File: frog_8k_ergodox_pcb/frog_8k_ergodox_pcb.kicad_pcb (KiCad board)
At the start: 2 copper layers, 344.7 x 123.6 mm, 214 parts, among them J1 USB_C_Receptacle_USB2.0_14P, J10 Conn_01x01_Pin, J2 Conn_01x04_Pin, J3 Conn_01x01_Pin, J4 Conn_01x01_Pin, J5 Conn_01x01_Pin, J6 Conn_01x01_Pin, J7 Conn_01x01_Pin, J8 Conn_01x01_Pin, J9 Conn_01x01_Pin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

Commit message: Connect PMW3360 pins.
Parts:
- moved R7 45.0 mm to (363.0, 117.2), turned to 0 degrees
- moved C1 29.1 mm to (343.8, 152.5)
- moved C2 27.0 mm to (343.8, 150.2)
- moved C3 7.79 mm to (337.8, 154.2)
- moved U3 6.57 mm to (343.0, 156.8)
- moved C4 6.45 mm to (344.2, 161.8)
- moved R3 5.15 mm to (364.5, 151.2), turned to 0 degrees
- moved R1 2.61 mm to (344.8, 143.2)
- moved R2 1.25 mm to (365.5, 137.2), turned to -45 degrees
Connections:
- C3 pad 1: V_{IN 3.3V} -> +3V3
- R1 pad 1: V_{IO VDD~3.3V} -> +3V3
- R2 pad 1: V_{IO VDD~3.3V} -> +3V3
- U1 pad 5: V_{IO VDD~3.3V} -> +3V3
- U3 pad 1: V_{IN 3.3V} -> +3V3
- U3 pad 3: V_{IN 3.3V} -> +3V3
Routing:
- net +3V3: track 64.8 -> 153.5 mm, vias 0 -> 2
- net VDD_{1.8V~2.1V}: track 0.00 -> 51.8 mm
- net Net-(U1-VDDPIX): track 0.00 -> 8.92 mm
- net Net-(U1-LED_P): track 0.00 -> 3.52 mm
- net Net-(U1-~{RESET}): track 6.34 -> 3.59 mm
- net MISO_{GPIO-PMW3360}: track 47.1 -> 44.7 mm
- net BOOT-1: track 12.9 -> 14.9 mm
- net CS_{GPIO-PMW3360}: track 40.0 -> 38.6 mm, vias 2 -> 1
- net SCLK_{GPIO-PMW3360}: track 34.2 -> 33.2 mm

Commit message: Connected All nets.
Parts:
- moved J3 53.1 mm to (330.0, 159.5)
- moved J5 52.6 mm to (327.0, 159.5)
- moved J7 52.1 mm to (324.0, 159.5)
- moved J9 51.7 mm to (321.0, 159.5)
- moved J4 32.5 mm to (330.0, 163.5)
- moved J10 32.5 mm to (321.0, 163.5)
- moved J6 32.5 mm to (327.0, 163.5)
- moved J8 32.5 mm to (324.0, 163.5)
- moved C4 1.90 mm to (342.5, 161.0), turned to -135 degrees
- moved C11 1.06 mm to (352.0, 128.2)
- moved C7 0.69 mm to (341.2, 124.5)
- moved C8 0.35 mm to (345.8, 115.5)
- moved C9 0.31 mm to (354.5, 119.8)
- turned C6 to 0 degrees
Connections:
- U2 pad 10: COL16 -> ADD2
- U2 pad 11: COL15 -> ADD4
- U2 pad 12: ROW5 -> ADD6
- U2 pad 18: COL0 -> COL11
- U2 pad 19: COL1 -> COL10
- U2 pad 2: ROW2 -> ADD7
- U2 pad 20: COL2 -> COL9
- U2 pad 21: COL10 -> COL8
- U2 pad 22: COL11 -> COL7
- U2 pad 25: ADD7 -> COL6
- U2 pad 26: ADD6 -> COL5
- U2 pad 27: ADD5 -> COL4
- U2 pad 28: ADD4 -> COL3
- U2 pad 29: ADD3 -> COL2
- U2 pad 3: ROW3 -> ADD5
- U2 pad 30: ADD2 -> COL1
- U2 pad 31: ADD1 -> COL0
- U2 pad 34: ADD0 -> ROW0
- U2 pad 37: COL14 -> COL13
- U2 pad 38: COL13 -> COL14
- U2 pad 39: COL3 -> COL15
- U2 pad 4: ROW4 -> ADD3
- U2 pad 40: COL4 -> COL16
- U2 pad 41: COL5 -> ROW5
- U2 pad 42: COL6 -> ROW4
- U2 pad 43: COL7 -> ROW3
- U2 pad 45: COL8 -> ROW2
- U2 pad 46: COL9 -> ROW1
- U2 pad 5: ROW0 -> ADD1
- U2 pad 6: ROW1 -> ADD0
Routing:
- net COL0: track 103.5 -> 427.4 mm, vias 0 -> 3
- net COL1: track 58.7 -> 366.3 mm, vias 0 -> 3
- net COL2: track 105.9 -> 388.9 mm, vias 0 -> 3
- net COL3: track 105.7 -> 368.9 mm, vias 0 -> 3
- net COL4: track 104.9 -> 347.1 mm, vias 0 -> 3
- net COL5: track 105.4 -> 326.1 mm, vias 0 -> 3
- net COL6: track 106.5 -> 303.7 mm, vias 0 -> 3
- net COL7: track 102.1 -> 276.1 mm, vias 0 -> 1
- net ROW5: track 315.4 -> 484.4 mm, vias 0 -> 2
- net ROW1: track 257.2 -> 425.0 mm, vias 0 -> 2
- net ROW4: track 317.1 -> 480.1 mm
- net COL8: track 103.3 -> 258.7 mm, vias 0 -> 1
- net ROW2: track 265.8 -> 417.2 mm, vias 0 -> 2
- net ROW3: track 259.7 -> 403.2 mm
- net COL9: track 103.1 -> 240.2 mm, vias 0 -> 1
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
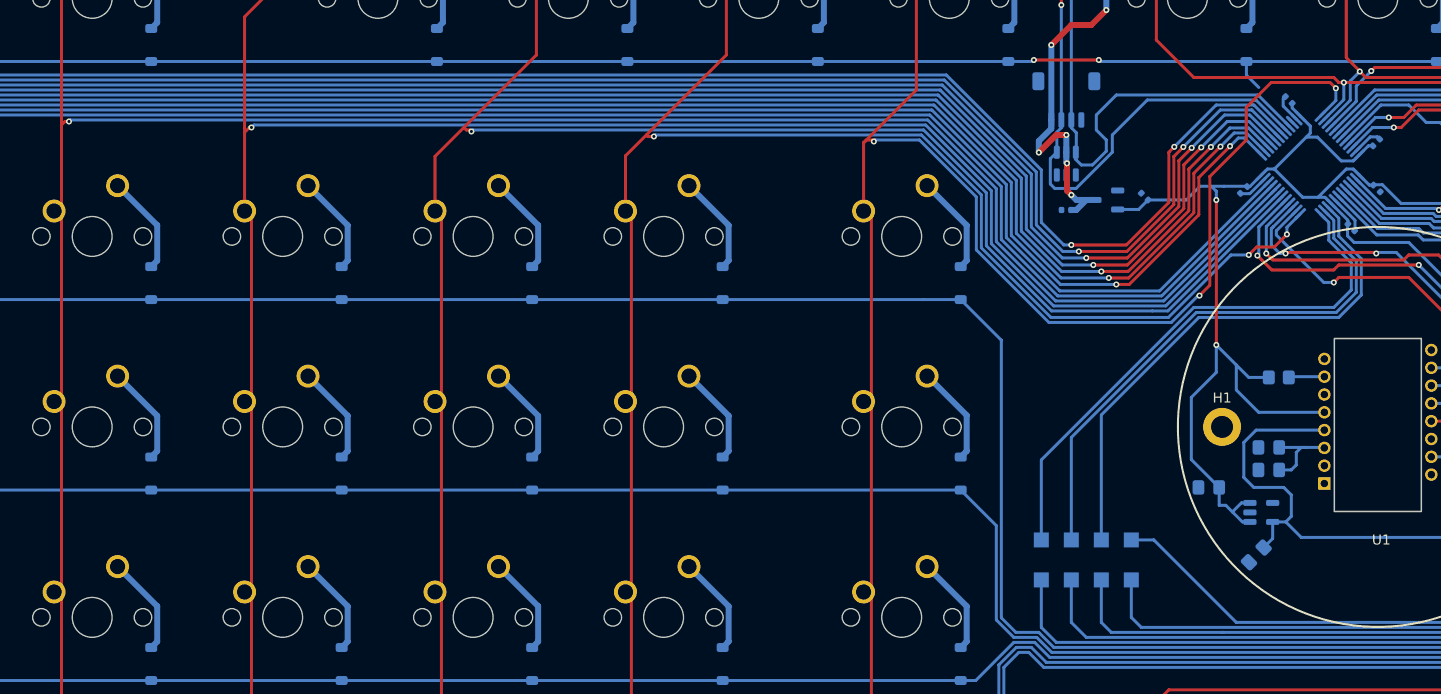
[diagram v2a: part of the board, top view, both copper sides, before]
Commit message: fixed connection little bit
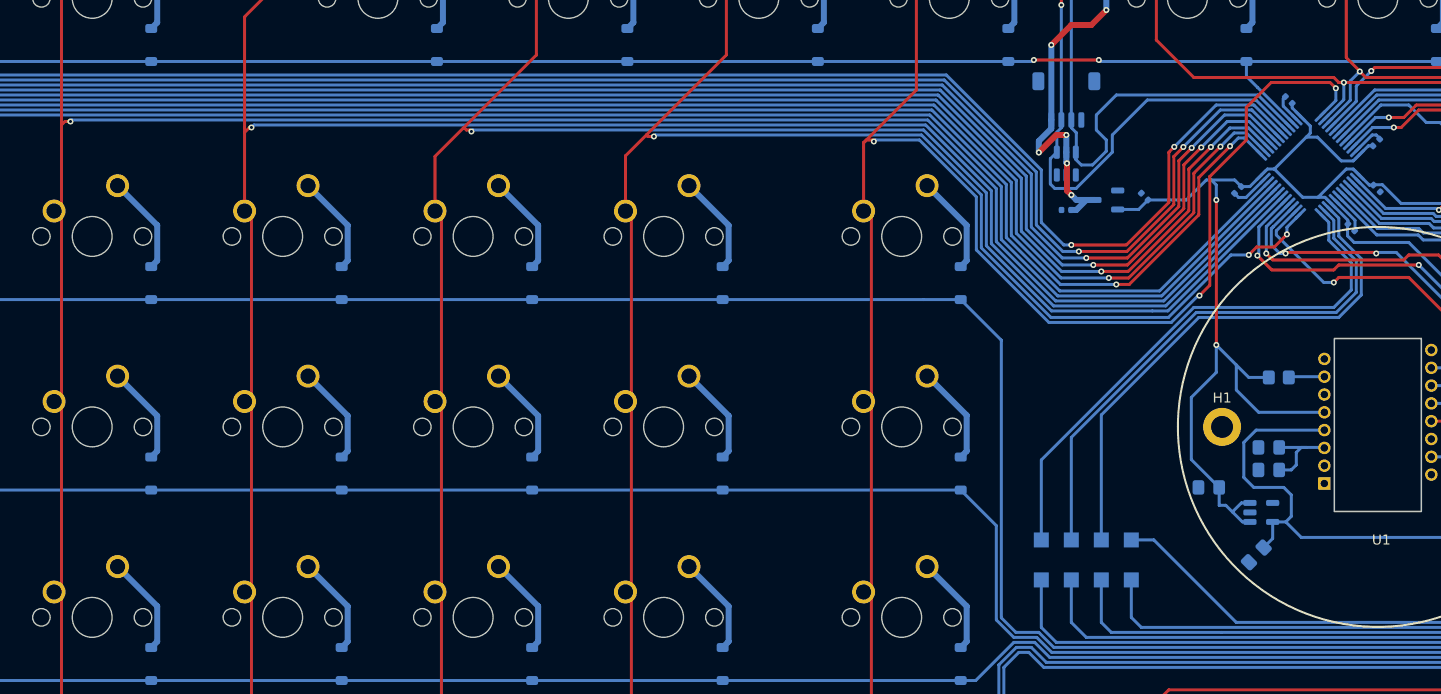
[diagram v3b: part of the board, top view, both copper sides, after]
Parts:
- moved C7 0.59 mm to (340.7, 124.5)
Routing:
- net ROW0: track 326.2 -> 330.4 mm
- net +3V3: track 147.3 -> 148.5 mm
- net GND: track 19.1 -> 20.2 mm

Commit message: Connect and fill ground.
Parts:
- moved C4 1.06 mm to (341.8, 160.2), turned to 180 degrees
- moved C12 1.00 mm to (323.5, 127.5)
- renumbered SW1 to BOOT, SW2 to RST
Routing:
- net ROW4: track 480.1 -> 477.5 mm
- net ROW5: track 484.4 -> 481.9 mm
- net +5V: track 35.5 -> 36.9 mm
- net MISO_{GPIO-PMW3360}: track 44.6 -> 45.9 mm
- net ROW3: track 403.2 -> 401.9 mm
- net ADD5: track 116.4 -> 115.3 mm
- net DN: track 61.2 -> 62.2 mm
- net DP: track 56.8 -> 55.9 mm
- net ADD7: track 120.9 -> 120.1 mm
- net ADD3: track 111.5 -> 110.8 mm
- net VDD_{1.8V~2.1V}: track 51.6 -> 52.2 mm
- net GND: track 20.2 -> 20.7 mm, vias 0 -> 13
- added copper zone on B.Cu, net GND
- added copper zone on F.Cu, net GND

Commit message: Almost Done with pcb
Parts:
- added R4: R1_10k, Resistor_SMD:R_0805_2012Metric_Pad1.20x1.40mm_HandSolder, B.Cu at (344.8, 140.8)
- renumbered BOOT to SW1, RST to SW2
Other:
- board text added: "A0"
- board text added: "A1"
- board text added: "A2"
- board text added: "Boot"
- board text added: "C13"
- board text added: "C14"
- board text added: "C15"
- board text added: "Designed by My-Fi"
- board text added: "F0"
- board text added: "F1"
- board text added: "Reset"

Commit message: Released V1.0.00
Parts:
- added mouse-bite-custom: VAL**, Mouse-Bites:mouse-bite-custom, F.Cu at (327.5, 98.5)
- added mouse-bite-custom: VAL**, Mouse-Bites:mouse-bite-custom, F.Cu at (320.0, 98.5)
- moved R5 1.25 mm to (320.5, 101.8)
- moved F1 1.10 mm to (327.5, 103.1)
- moved R6 0.75 mm to (325.0, 101.8)
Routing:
- net VBUS: track 11.8 -> 13.2 mm
- net Net-(J1-CC2): track 3.46 -> 4.67 mm
- net +5V: track 36.9 -> 35.8 mm
- net Net-(J1-CC1): track 3.31 -> 4.06 mm
- net GND: vias 13 -> 14
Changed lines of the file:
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@@
 		)
 	)
+	(footprint "Mouse-Bites:mouse-bite-custom"
+		(layer "F.Cu")
+		(at 327.5 98.5)
+		(property "Reference" "mouse-bite-custom"
+			(at 0 -1.5 0)
+			(layer "F.SilkS")
+			(hide yes)
+			(effects
+				(font
+					(size 1 1)
+					(thickness 0.2)
+				)
+			)
+		)
+		(property "Value" "VAL**"
+			(at 0 1 0)
+			(layer "F.SilkS")
+			(hide yes)
+			(effects
+				(font
+					(size 1 1)
+					(thickness 0.2)
+				)
+			)
+		)
+		(property "Footprint" "Mouse-Bites:custom"
+			(at -0.5 -3.5 0)
+			(layer "F.Fab")
+			(hide yes)
+			(effects
+				(font
+					(size 1.27 1.27)
+					(thickness 0.15)
+				)
+			)
+		)
+		(property "Datasheet" ""
+			(at 0 0 0)
+			(layer "F.Fab")
+			(hide yes)
+			(effects
+				(font
+					(size 1.27 1.27)
+					(thickness 0.15)
+				)
+			)
+		)
+		(property "Description" ""
+			(at 0 0 0)
+			(layer "F.Fab")
+			(hide yes)
+			(effects
+				(font
+					(size 1.27 1.27)
+					(thickness 0.15)
+				)
+			)
+		)
+		(attr through_hole)
+		(pad "" np_thru_hole circle
+			(at -0.75 0)
+			(size 0.5 0.5)
+			(drill 0.5)
+			(layers "F&B.Cu" "*.Mask")
+		)
+		(pad "" np_thru_hole circle
+			(at 0 0)
+			(size 0.5 0.5)
+			(drill 0.5)
+			(layers "F&B.Cu" "*.Mask")
+		)
+		(pad "" np_thru_hole circle
+			(at 0.75 0)
+			(size 0.5 0.5)
+			(drill 0.5)
+			(layers "F&B.Cu" "*.Mask")
+		)
+	)
 	(footprint "PCM_marbastlib-mx:SW_MX_1u"
 		(layer "F.Cu")
@@
 		)
 	)
+	(footprint "Mouse-Bites:mouse-bite-custom"
+		(layer "F.Cu")
+		(at 320 98.5)
+		(property "Reference" "mouse-bite-custom"
+			(at 0 -1.5 0)
+			(layer "F.SilkS")
+			(hide yes)
+			(effects
+				(font
+					(size 1 1)
+					(thickness 0.2)
+				)
+			)
+		)
+		(property "Value" "VAL**"
+			(at 0 1 0)
+			(layer "F.SilkS")
+			(hide yes)
+			(effects
+				(font
+					(size 1 1)
+					(thickness 0.2)
+				)
+			)
+		)
+		(property "Footprint" "Mouse-Bites:custom"
+			(at -0.5 -3.5 0)
+			(layer "F.Fab")
+			(hide yes)
+			(effects
+				(font
+					(size 1.27 1.27)
+					(thickness 0.15)
+				)
+			)
+		)
+		(property "Datasheet" ""
+			(at 0 0 0)
+			(layer "F.Fab")
+			(hide yes)
+			(effects
+				(font
+					(size 1.27 1.27)
+					(thickness 0.15)
+				)
+			)
+		)
+		(property "Description" ""
+			(at 0 0 0)
+			(layer "F.Fab")
+			(hide yes)
+			(effects
+				(font
+					(size 1.27 1.27)
+					(thickness 0.15)
+				)
+			)
+		)
+		(attr through_hole)
+		(pad "" np_thru_hole circle
+			(at -0.75 0)
+			(size 0.5 0.5)
+			(drill 0.5)
+			(layers "*.Cu" "*.Mask")
+		)
+		(pad "" np_thru_hole circle
+			(at 0 0)
+			(size 0.5 0.5)
+			(drill 0.5)
+			(layers "*.Cu" "*.Mask")
+		)
+		(pad "" np_thru_hole circle
+			(at 0.75 0)
+			(size 0.5 0.5)
+			(drill 0.5)
+			(layers "*.Cu" "*.Mask")
+		)
+	)
 	(footprint "PCM_marbastlib-mx:SW_MX_1u"
 		(layer "F.Cu")
@@
 	(footprint "Fuse:Fuse_1206_3216Metric"
 		(layer "B.Cu")
-		(at 327.5 102 -90)
+		(at 327.5 103.100001 -90)
 		(descr "Fuse SMD 1206 (3216 Metric), square (rectangular) end terminal, IPC_7351 nominal, (Body size source: http://www.tortai-tech.com/upload/download/2011102023233369053.pdf), generated with kicad-footprint-generator")
 		(tags "fuse")
@@
 	(footprint "Resistor_SMD:R_0805_2012Metric_Pad1.20x1.40mm_HandSolder"
 		(layer "B.Cu")
-		(at 321.5 101 -90)
+		(at 320.5 101.75 -90)
 		(descr "Resistor SMD 0805 (2012 Metric), square (rectangular) end terminal, IPC_7351 nominal with elongated pad for handsoldering. (Body size source: IPC-SM-782 page 72, https://www.pcb-3d.com/wordpress/wp-content/uploads/ipc-sm-782a_amendment_1_and_2.pdf), generated with kicad-footprint-generator")
 		(tags "resistor handsolder")
@@
 	(footprint "Resistor_SMD:R_0805_2012Metric_Pad1.20x1.40mm_HandSolder"
 		(layer "B.Cu")
-		(at 325 101 -90)
+		(at 325 101.75 -90)
 		(descr "Resistor SMD 0805 (2012 Metric), square (rectangular) end terminal, IPC_7351 nominal with elongated pad for handsoldering. (Body size source: IPC-SM-782 page 72, https://www.pcb-3d.com/wordpress/wp-content/uploads/ipc-sm-782a_amendment_1_and_2.pdf), generated with kicad-footprint-generator")
 		(tags "resistor handsolder")
@@
 		(net 1)
 	)
+	(via
+		(at 328 97.5)
+		(size 0.6)
+		(drill 0.3)
+		(layers "F.Cu" "B.Cu")
+		(free yes)
+		(net 1)
+	)
 	(segment
 		(start 343.370059 123.352342)
@@
 	)
 	(segment
-		(start 327.5 103.399999)
-		(end 327.5 106.5)
+		(start 323.5 121.772509)
+		(end 323.564991 121.8375)
 		(width 0.6)
 		(layer "B.Cu")
@@
 	)
 	(segment
-		(start 323.5 121.772509)
-		(end 323.564991 121.8375)
+		(start 321.5 120)
+		(end 321.5 118.85576)
 		(width 0.6)
 		(layer "B.Cu")
@@
 	)
 	(segment
-		(start 321.5 120)
-		(end 321.5 118.85576)
+		(start 327.5 104.5)
+		(end 327.5 106.5)
 		(width 0.6)
 		(layer "B.Cu")
@@
 	)
 	(segment
-		(start 326.145 98.045)
+		(start 326.145 97.973629)
 		(end 326.145 96.72)
 		(width 0.6)
@@
 	)
 	(segment
+		(start 327.5 100.25)
+		(end 327.368628 100.25)
+		(width 0.6)
+		(layer "F.Cu")
+		(net 101)
+	)
+	(segment
+		(start 327.368628 100.25)
+		(end 325.805906 98.687278)
+		(width 0.6)
+		(layer "F.Cu")
+		(net 101)
+	)
+	(segment
 		(start 321.245 95.860305)
 		(end 321.245 96.72)
@@
 	)
 	(segment
-		(start 327.175 99.075)
-		(end 326.145 98.045)
+		(start 325.805906 98.687278)
+		(end 325.805906 98.312723)
+		(width 0.6)
+		(layer "F.Cu")
+		(net 101)
+	)
+	(segment
+		(start 325.805906 98.312723)
+		(end 326.145 97.973629)
 		(width 0.6)
 		(layer "F.Cu")
@@
 	)
 	(via
-		(at 327.175 99.075)
+		(at 327.5 100.25)
 		(size 0.6)
 		(drill 0.3)
@@
 	)
 	(segment
-		(start 327.5 99.4)
-		(end 327.5 100.600001)
-		(width 0.6)
-		(layer "B.Cu")
-		(net 101)
-	)
-	(segment
-		(start 327.175 99.075)
-		(end 327.5 99.4)
+		(start 327.5 100.25)
+		(end 327.5 101.700002)
 		(width 0.6)
 		(layer "B.Cu")
@@
 	(segment
 		(start 325 98.509364)
-		(end 325 100)
+		(end 325 100.75)
 		(width 0.3)
 		(layer "B.Cu")
@@
 	)
 	(segment
-		(start 321.945 96.72)
-		(end 321.945 98.055)
+		(start 321.945 98.945)
+		(end 321.945 96.72)
 		(width 0.3)
 		(layer "F.Cu")
@@
 	)
 	(segment
-		(start 321.945 98.055)
-		(end 321.5 98.5)
+		(start 322 99)
+		(end 321.945 98.945)
 		(width 0.3)
 		(layer "F.Cu")
@@
 	)
 	(via
-		(at 321.5 98.5)
+		(at 322 99)
 		(size 0.6)
 		(drill 0.3)
@@
 	)
 	(segment
-		(start 321.5 100)
-		(end 321.5 98.5)
+		(start 322 99.25)
+		(end 320.5 100.75)
+		(width 0.3)
+		(layer "B.Cu")
+		(net 106)
+	)
+	(segment
+		(start 322 99)
+		(end 322 99.25)
 		(width 0.3)
 		(layer "B.Cu")
